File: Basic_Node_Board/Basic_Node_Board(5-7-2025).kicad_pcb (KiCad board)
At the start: 2 copper layers, 62.5 x 82.5 mm, 24 parts, among them J1 Conn_01x02_Pin, J2 Conn_01x02, J3 Conn_01x19_Socket, J5 Conn_01x19_Socket, U1 INA220 Current Monitor, U2 ESP32-DEVKIT-C, U3 TJA1050T/CM,118, U6 AP64060WU-7

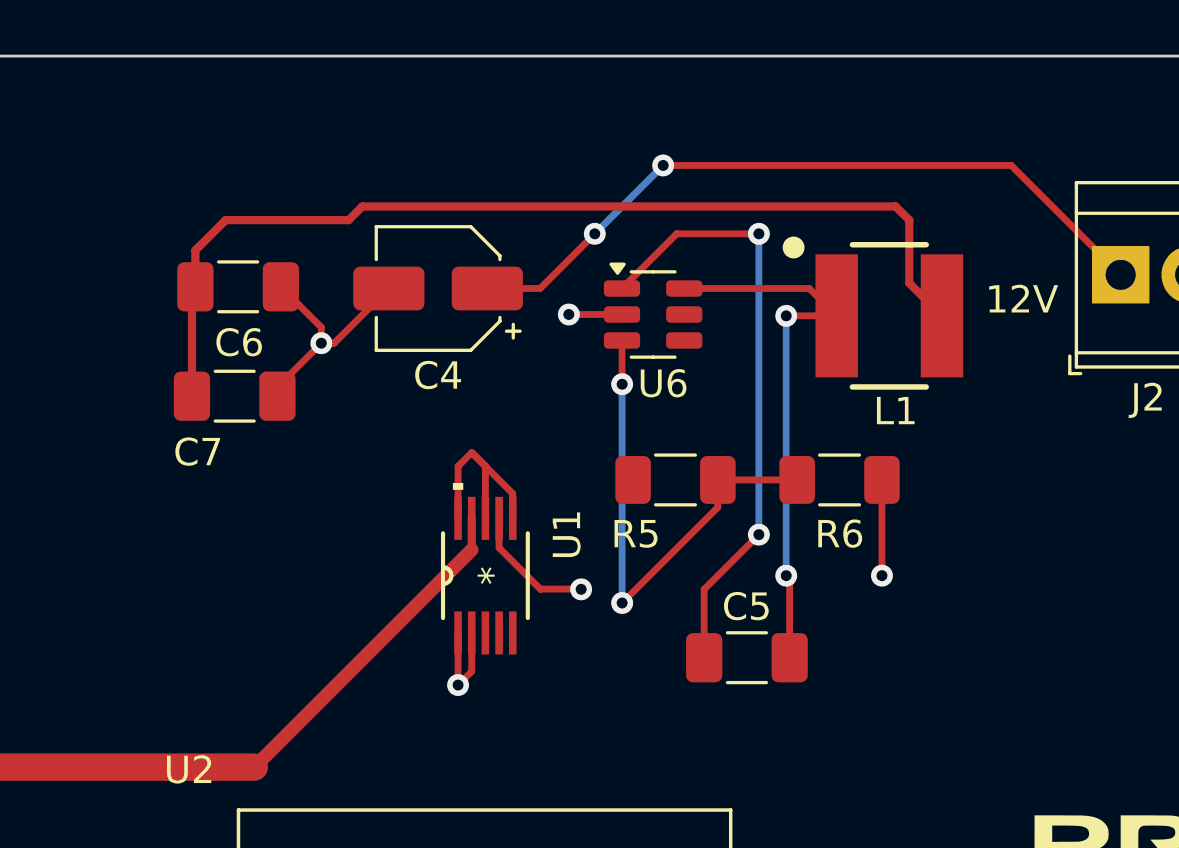
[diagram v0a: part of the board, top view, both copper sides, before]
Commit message: Adding Buck Converter Schematic/Footprints
Added footprints to main pcb. Removing duplicate footprints (might cause problems, we will find out).
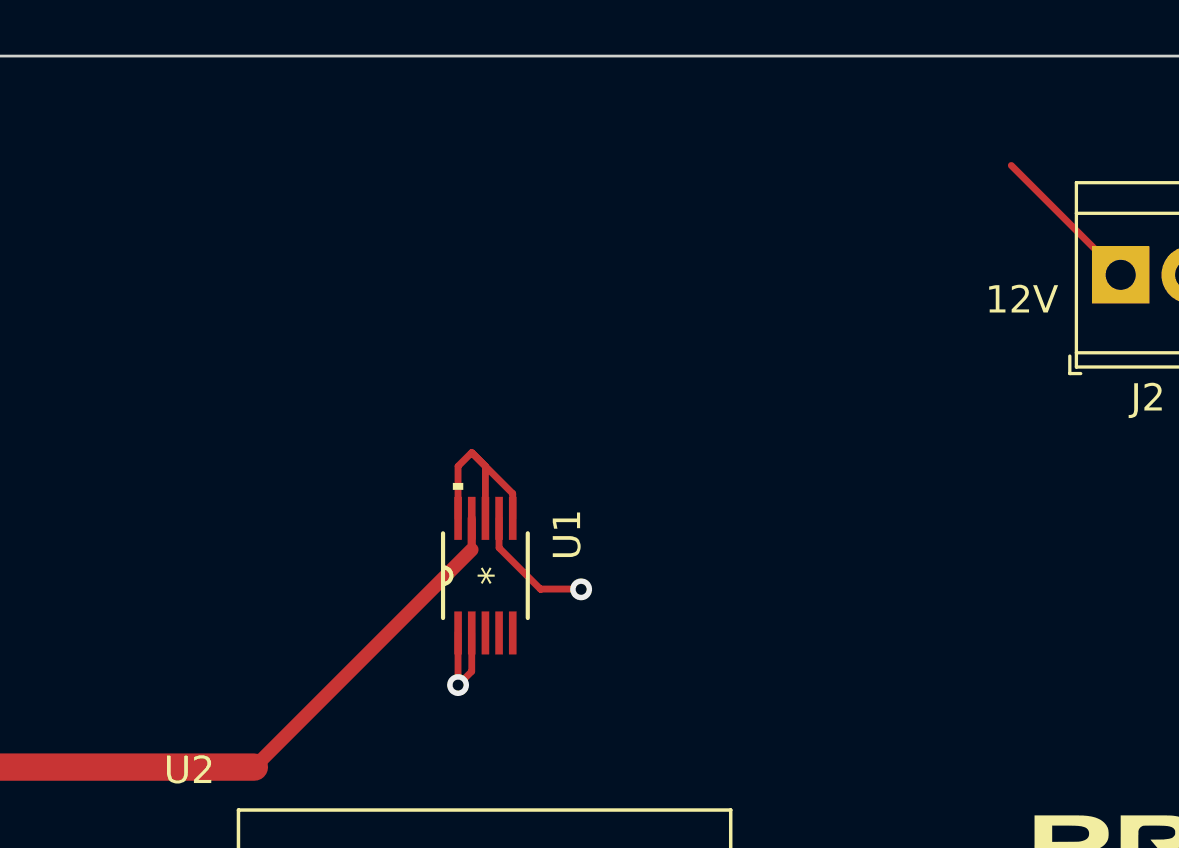
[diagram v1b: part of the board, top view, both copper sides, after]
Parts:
- removed C4: 2.2u, Capacitor_SMD:CP_Elec_4x5.4
- removed C5: 0.1u, Capacitor_SMD:C_1206_3216Metric_Pad1.33x1.80mm_HandSolder
- removed C6, C7: 10u, Capacitor_SMD:C_1206_3216Metric_Pad1.33x1.80mm_HandSolder
- removed L1: 10u, PROVE:WE-LQS_5040
- removed R5: 115k, Resistor_SMD:R_1206_3216Metric_Pad1.30x1.75mm_HandSolder
- removed R6: 22.1k, Resistor_SMD:R_1206_3216Metric_Pad1.30x1.75mm_HandSolder
- removed U6: AP64060WU-7, Package_TO_SOT_SMD:TSOT-23-6
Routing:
- net /Microcontroller/BUCK_5V: track 36.4 -> 0.00 mm
- net Net-(U6-BST): track 22.2 -> 0.00 mm, vias 2 -> 0
- net /Power_Supply/12V_IN: track 26.7 -> 5.66 mm, vias 2 -> 0
- net Net-(U6-SW): track 20.4 -> 0.00 mm, vias 2 -> 0
- net Net-(U6-FB): track 18.5 -> 0.00 mm, vias 2 -> 0
- net GND: track 43.8 -> 29.6 mm, vias 9 -> 6
